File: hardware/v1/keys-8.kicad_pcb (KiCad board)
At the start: 2 copper layers, 101 x 36.2 mm, 13 parts, among them P1 CONN_02X02, P2 CONN_01X03, P3 CONN_01X03, P4 CONN_01X03, SW1 SWITCH_INV, SW2 SWITCH_INV, SW3 SWITCH_INV, SW4 SWITCH_INV, SW5 SWITCH_INV, SW6 SWITCH_INV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

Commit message: replace switch footprints on keys-8
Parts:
- SW1, SW2, SW3, SW4, SW5, SW6, SW7, SW8: footprint myparts:SW_SPDT -> myparts:SW_SPDT-custom

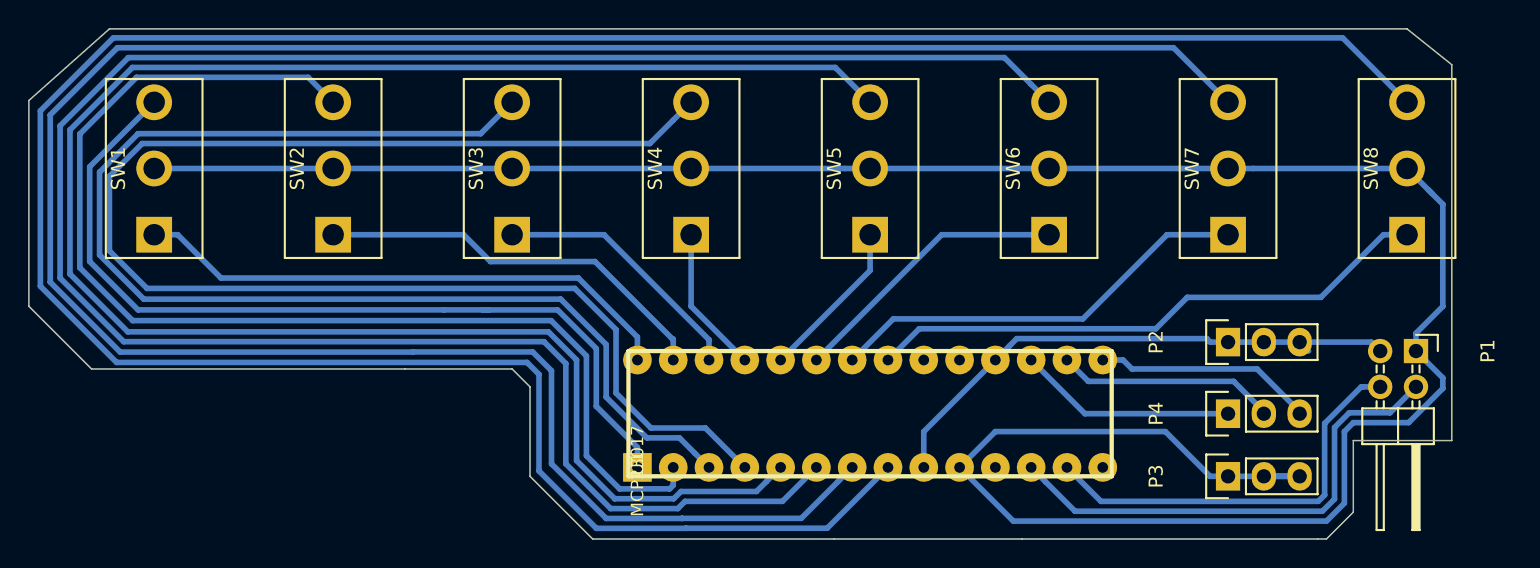
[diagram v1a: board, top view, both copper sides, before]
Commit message: slightly re-route keys-8 to shave off a few mm. Re-export gerber files and svg (edge.cuts and b.fab) to put into a new front panel cutting file.
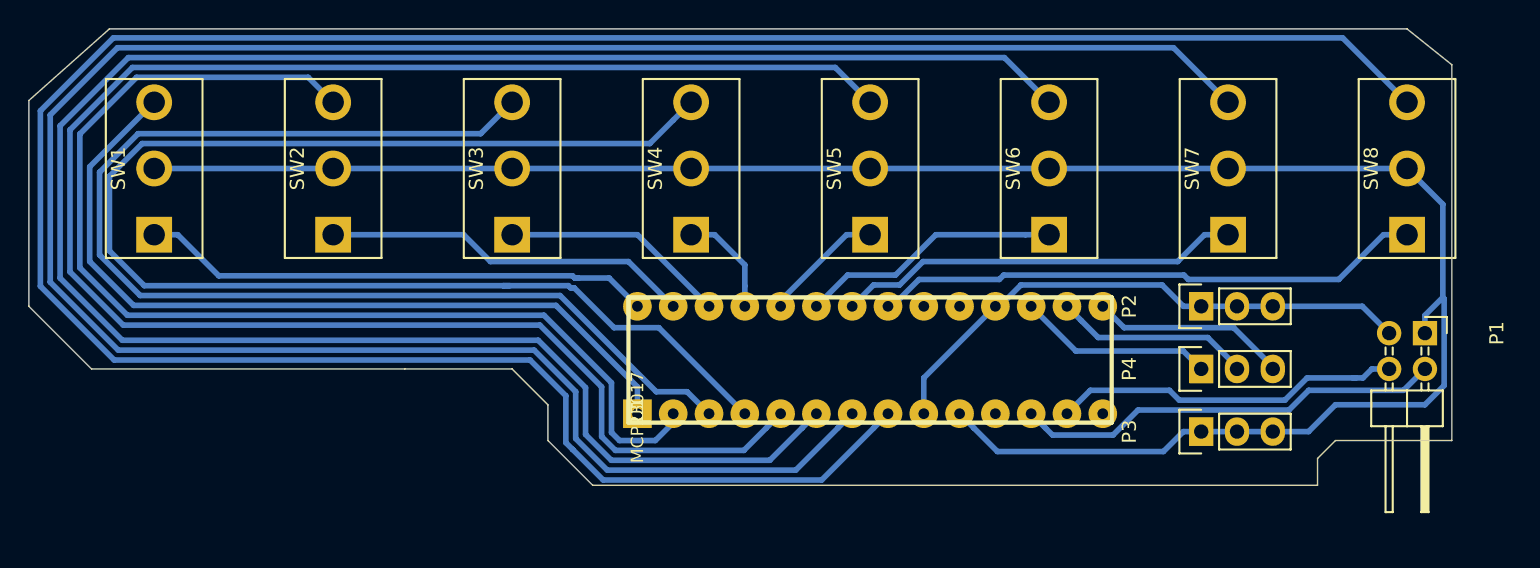
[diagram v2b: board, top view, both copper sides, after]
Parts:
- moved U1 3.81 mm to (174.0, 94.6)
- moved P3 3.70 mm to (214.0, 95.9)
- moved P4 3.70 mm to (214.0, 91.4)
- moved P2 3.17 mm to (214.0, 87.0)
- moved P1 1.42 mm to (229.9, 88.9)
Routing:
- net GND: track 179.3 -> 145.9 mm
- net /SCK: track 35.2 -> 30.5 mm
- net /SDA: track 29.6 -> 24.9 mm
- net Net-(SW3-Pad3): track 88.9 -> 85.1 mm
- net Net-(SW4-Pad3): track 102.8 -> 99.1 mm
- net Net-(SW2-Pad3): track 84.0 -> 80.3 mm
- net Net-(SW1-Pad3): track 61.8 -> 58.3 mm
- net Net-(SW6-Pad3): track 150.1 -> 146.6 mm
- net Net-(SW5-Pad3): track 132.0 -> 128.5 mm
- net Net-(SW8-Pad3): track 186.5 -> 183.2 mm
- net Net-(SW7-Pad3): track 168.2 -> 165.1 mm
- net Net-(SW4-Pad1): track 10.5 -> 7.64 mm
- net Net-(SW5-Pad1): track 11.5 -> 8.69 mm
- net Net-(SW2-Pad1): track 28.8 -> 26.2 mm
- net Net-(SW3-Pad1): track 18.5 -> 16.1 mm
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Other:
- board size 101 x 36.2 mm -> 101 x 32.4 mm
